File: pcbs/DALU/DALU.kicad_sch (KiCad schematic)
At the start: 0 parts

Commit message: Starting to think about decoding etc.
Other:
- added sheet Decoder (Decoder.kicad_sch)

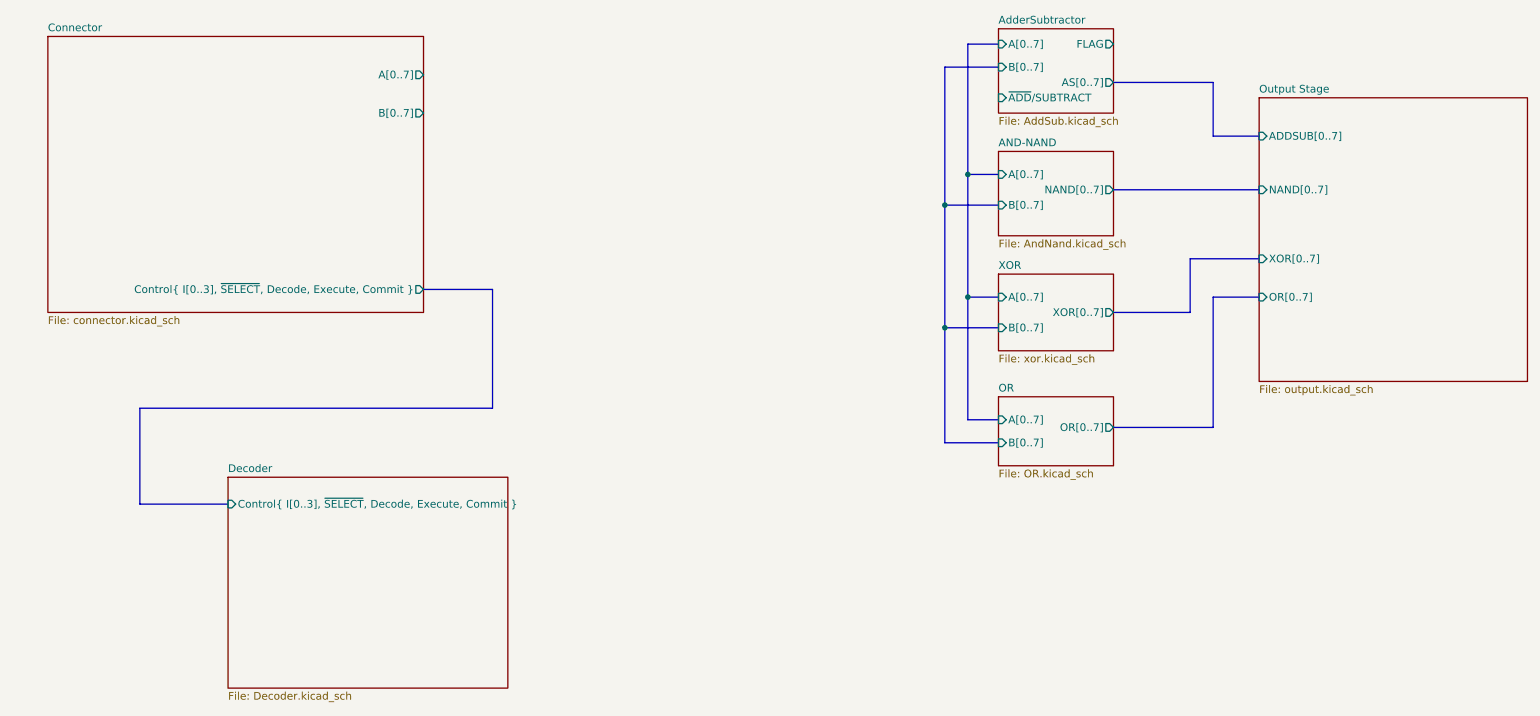
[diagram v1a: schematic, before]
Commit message: Starting to do the routing. Schematic not yet complete, though
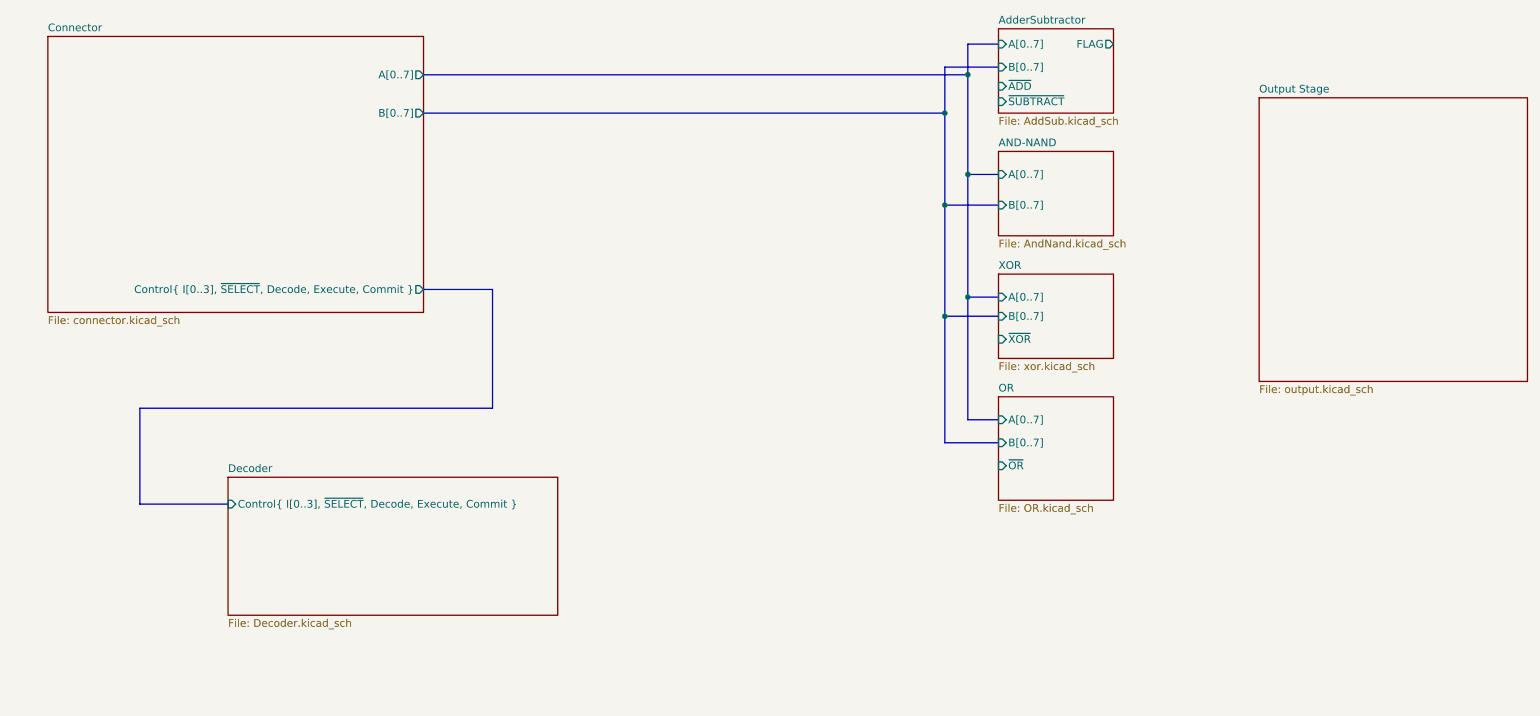
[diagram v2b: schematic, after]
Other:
- sheet AND-NAND ports: added none; removed NAND[0..7]
- sheet AdderSubtractor ports: added ~{ADD}, ~{SUBTRACT}; removed AS[0..7], ~{ADD}/SUBTRACT
- sheet OR ports: added ~{OR}; removed OR[0..7]
- sheet Output Stage ports: added none; removed ADDSUB[0..7], NAND[0..7], OR[0..7], XOR[0..7]
- sheet XOR ports: added ~{XOR}; removed XOR[0..7]

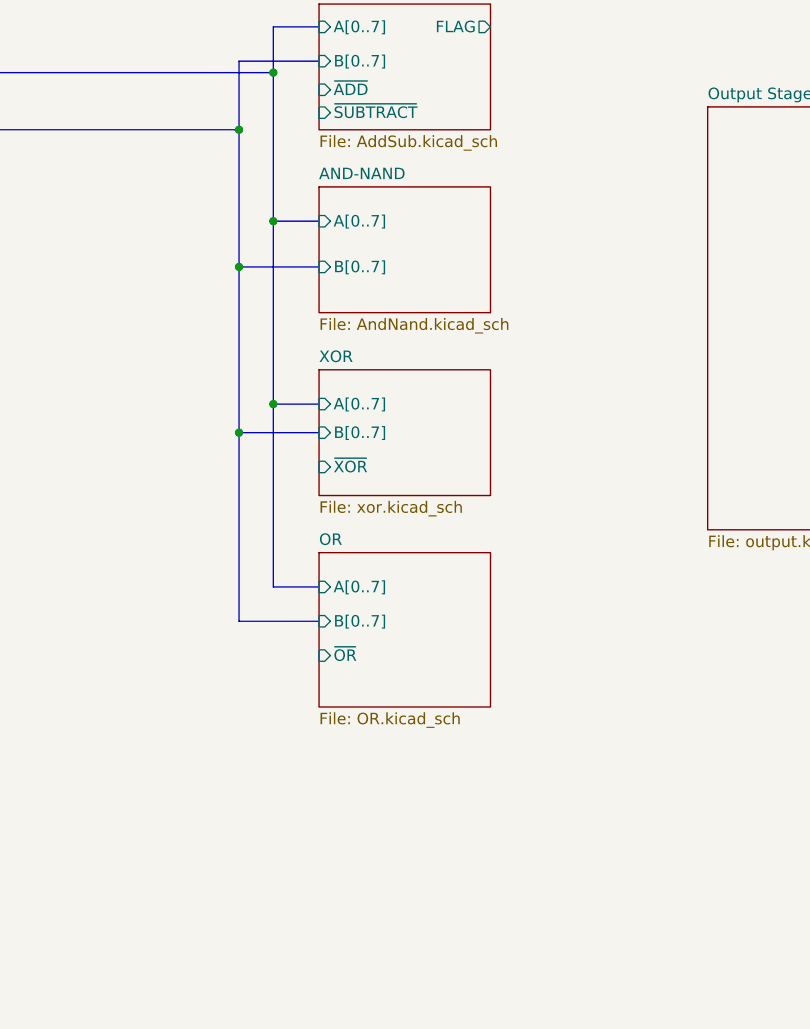
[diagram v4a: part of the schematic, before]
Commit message: Separate out AND stage
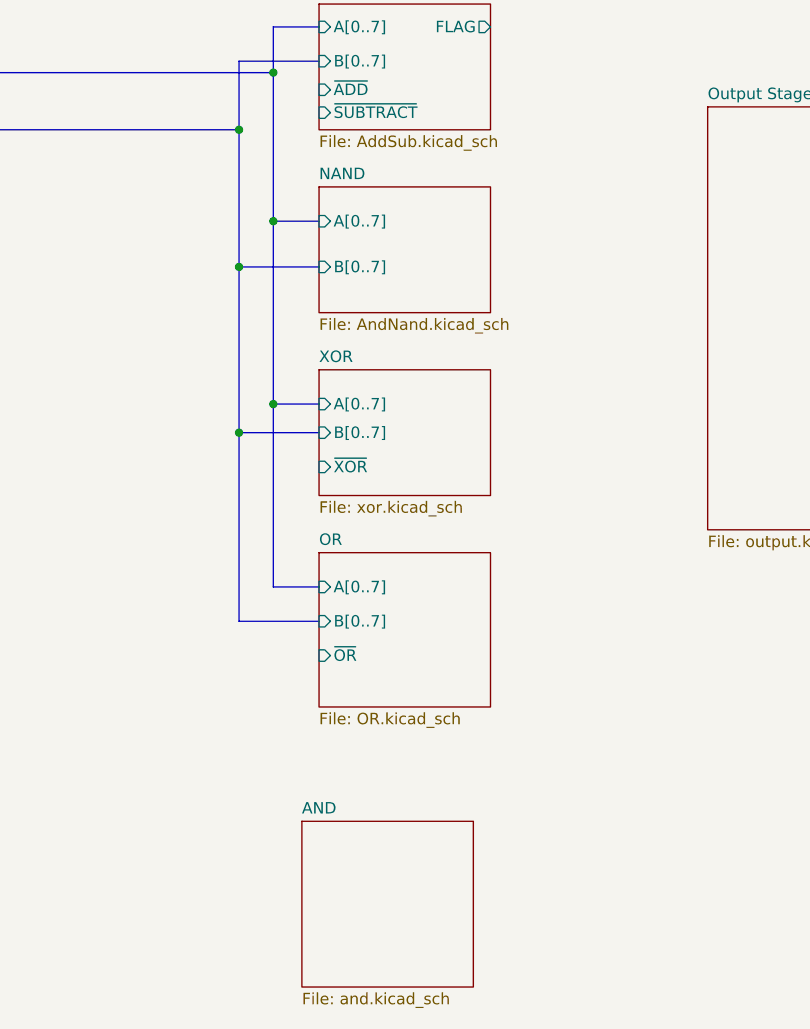
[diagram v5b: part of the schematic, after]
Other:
- sheet AND-NAND renamed NAND
- added sheet AND (and.kicad_sch)

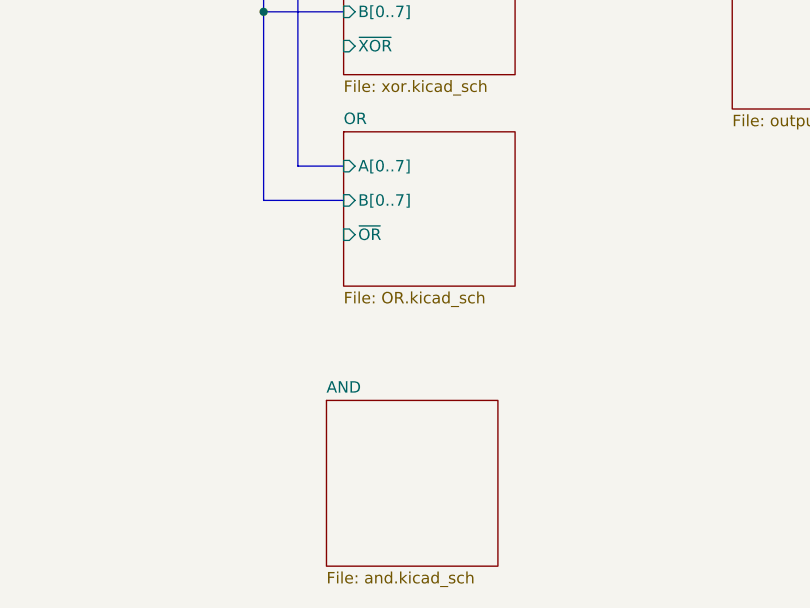
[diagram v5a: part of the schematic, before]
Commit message: Routing.... have realised that I need to think more about vias
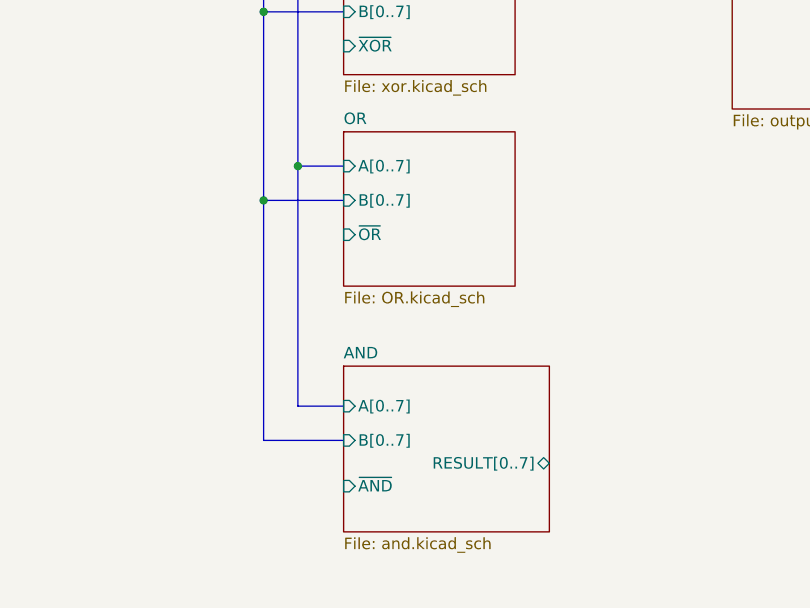
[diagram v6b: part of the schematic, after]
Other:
- sheet AND ports: added A[0..7], B[0..7], RESULT[0..7], ~{AND}; removed none
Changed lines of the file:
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@@
   (paper "A4")
   (bus_alias "A" (members "A"))
+  (junction (at 184.15 97.79) (diameter 0) (color 0 0 0 0)
+  )
   (junction (at 180.34 46.99) (diameter 0) (color 0 0 0 0)
   )
@@
   (junction (at 184.15 57.15) (diameter 0) (color 0 0 0 0)
   )
+  (junction (at 180.34 101.6) (diameter 0) (color 0 0 0 0)
+  )
   (junction (at 184.15 40.64) (diameter 0) (color 0 0 0 0)
   )
@@
     (stroke (width 0) (type default) (color 0 0 0 0))
   )
+  (bus (pts (xy 180.34 128.27) (xy 180.34 101.6))
+    (stroke (width 0) (type default) (color 0 0 0 0))
+  )
   (bus (pts (xy 93.98 76.2) (xy 105.41 76.2))
     (stroke (width 0) (type default) (color 0 0 0 0))
@@
     (stroke (width 0) (type default) (color 0 0 0 0))
   )
+  (bus (pts (xy 189.23 124.46) (xy 184.15 124.46))
+    (stroke (width 0) (type default) (color 0 0 0 0))
+  )
   (bus (pts (xy 180.34 101.6) (xy 189.23 101.6))
     (stroke (width 0) (type default) (color 0 0 0 0))
@@
     (stroke (width 0) (type default) (color 0 0 0 0))
   )
+  (bus (pts (xy 189.23 128.27) (xy 180.34 128.27))
+    (stroke (width 0) (type default) (color 0 0 0 0))
+  )
   (bus (pts (xy 46.99 111.76) (xy 61.595 111.76))
     (stroke (width 0) (type default) (color 0 0 0 0))
@@
   )
   (bus (pts (xy 180.34 62.23) (xy 180.34 46.99))
+    (stroke (width 0) (type default) (color 0 0 0 0))
+  )
+  (bus (pts (xy 184.15 97.79) (xy 184.15 124.46))
     (stroke (width 0) (type default) (color 0 0 0 0))
   )
@@
     )
   )
-  (sheet (at 187.325 123.825) (size 19.05 18.415) (fields_autoplaced)
+  (sheet (at 189.23 120.015) (size 22.86 18.415) (fields_autoplaced)
     (stroke (width 0.1524) (type solid) (color 0 0 0 0))
     (fill (color 0 0 0 0.0000))
-    (property "Sheet name" "AND" (id 0) (at 187.325 123.1134 0)
+    (property "Sheet name" "AND" (id 0) (at 189.23 119.3034 0)
       (effects (font (size 1.27 1.27)) (justify left bottom))
     )
-    (property "Sheet file" "and.kicad_sch" (id 1) (at 187.325 142.8246 0)
+    (property "Sheet file" "and.kicad_sch" (id 1) (at 189.23 139.0146 0)
       (effects (font (size 1.27 1.27)) (justify left top))
+    )
+    (pin "A[0..7]" input (at 189.23 124.46 180)
+      (effects (font (size 1.27 1.27)) (justify left))
+    )
+    (pin "B[0..7]" input (at 189.23 128.27 180)
+      (effects (font (size 1.27 1.27)) (justify left))
+    )
+    (pin "~{AND}" input (at 189.23 133.35 180)
+      (effects (font (size 1.27 1.27)) (justify left))
+    )
+    (pin "RESULT[0..7]" tri_state (at 212.09 130.81 0)
+      (effects (font (size 1.27 1.27)) (justify right))
     )
   )
@@
       (reference "#FLG0202") (unit 1) (value "PWR_FLAG") (footprint "")
     )
+    (path "/95c8ed90-5067-42ef-af82-1a4d464a971b/b6b93ce5-aa23-45e8-b2af-b087ca6b9d48"
+      (reference "#PWR0101") (unit 1) (value "+5V") (footprint "")
+    )
+    (path "/95c8ed90-5067-42ef-af82-1a4d464a971b/9db16e8b-0d8b-476f-9566-5fdb7a2ac4e3"
+      (reference "#PWR0102") (unit 1) (value "GND") (footprint "")
+    )
     (path "/5a7cb513-9739-4d2d-a582-8607360c12f9/80b492a5-fd4d-44b4-9dea-06998740736c"
       (reference "#PWR0201") (unit 1) (value "GND") (footprint "")
@@
       (reference "#PWR0607") (unit 1) (value "GND") (footprint "")
     )
+    (path "/95c8ed90-5067-42ef-af82-1a4d464a971b/67209d39-ed0c-425f-b805-1ccb7d9f82f1"
+      (reference "#PWR0701") (unit 1) (value "+5V") (footprint "")
+    )
+    (path "/95c8ed90-5067-42ef-af82-1a4d464a971b/2db216d7-3b2d-4871-b8fa-6637d71c995d"
+      (reference "#PWR0702") (unit 1) (value "GND") (footprint "")
+    )
     (path "/95c8ed90-5067-42ef-af82-1a4d464a971b/57d3caed-aea1-4b83-9b7e-e1305c1c7376"
-      (reference "#PWR0701") (unit 1) (value "+5V") (footprint "")
+      (reference "#PWR0703") (unit 1) (value "+5V") (footprint "")
     )
     (path "/95c8ed90-5067-42ef-af82-1a4d464a971b/0917cb94-2f6f-428c-a831-dad7148e5959"
-      (reference "#PWR0702") (unit 1) (value "+5V") (footprint "")
+      (reference "#PWR0704") (unit 1) (value "+5V") (footprint "")
     )
     (path "/95c8ed90-5067-42ef-af82-1a4d464a971b/89b20fcd-56a0-4837-890b-7efca74737e5"
-      (reference "#PWR0703") (unit 1) (value "GND") (footprint "")
+      (reference "#PWR0705") (unit 1) (value "GND") (footprint "")
     )
     (path "/c0fae5e0-fcfe-44dd-9b04-acaebbeafed8/e7c6e0ab-5e50-42d6-98ef-0ae6448d2add"
@@
       (reference "#PWR0811") (unit 1) (value "GND") (footprint "")
     )
+    (path "/f9fa4380-5207-468c-92a9-e91d22c563ae/3c317aa0-86a1-4b22-bf10-b4b691996464"
+      (reference "#PWR0901") (unit 1) (value "+5V") (footprint "")
+    )
     (path "/f9fa4380-5207-468c-92a9-e91d22c563ae/3a411b23-6b77-4577-aaea-6ef1cb2fcfad"
-      (reference "#PWR?") (unit 1) (value "+5V") (footprint "")
-    )
-    (path "/f9fa4380-5207-468c-92a9-e91d22c563ae/3c317aa0-86a1-4b22-bf10-b4b691996464"
-      (reference "#PWR?") (unit 1) (value "+5V") (footprint "")
+      (reference "#PWR0902") (unit 1) (value "+5V") (footprint "")
     )
     (path "/f9fa4380-5207-468c-92a9-e91d22c563ae/a8fa920f-f5c4-48d9-8981-d16703c150d0"
-      (reference "#PWR?") (unit 1) (value "GND") (footprint "")
+      (reference "#PWR0903") (unit 1) (value "GND") (footprint "")
+    )
+    (path "/95c8ed90-5067-42ef-af82-1a4d464a971b/1f024bff-4ccc-4a0d-8969-9176c09b87da"
+      (reference "C701") (unit 1) (value "100n") (footprint "Capacitor_SMD:C_0603_1608Metric")
+    )
+    (path "/95c8ed90-5067-42ef-af82-1a4d464a971b/82621a0e-287e-428f-9f23-64fcd965f942"
+      (reference "C702") (unit 1) (value "100n") (footprint "Capacitor_SMD:C_0603_1608Metric")
+    )
+    (path "/95c8ed90-5067-42ef-af82-1a4d464a971b/45b91593-1fee-4f04-932d-bd095ba5b8e2"
+      (reference "C703") (unit 1) (value "100n") (footprint "Capacitor_SMD:C_0603_1608Metric")
     )
     (path "/d3da35c4-2e12-46e3-ad1e-753dacdb708b/8a1c4a3d-ca7d-42e4-b51b-a7510e9bc529"
@@
     )
     (path "/f9fa4380-5207-468c-92a9-e91d22c563ae/f846c315-bd19-4d55-8e50-0deec05b9208"
-      (reference "U?") (unit 1) (value "74HC245") (footprint "Package_SO:SOIC-20W_7.5x12.8mm_P1.27mm")
-    )
-  )
+      (reference "U903") (unit 1) (value "74HC245") (footprint "Package_SO:SOIC-20W_7.5x12.8mm_P1.27mm")
+    )
+  )
